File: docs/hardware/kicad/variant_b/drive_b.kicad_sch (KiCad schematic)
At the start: 11 parts, among them U40 74LVC08, U41 MDD20A front, U42 MDD20A rear, U43 CS FL, U44 CS FR, U45 CS RL, U46 CS RR

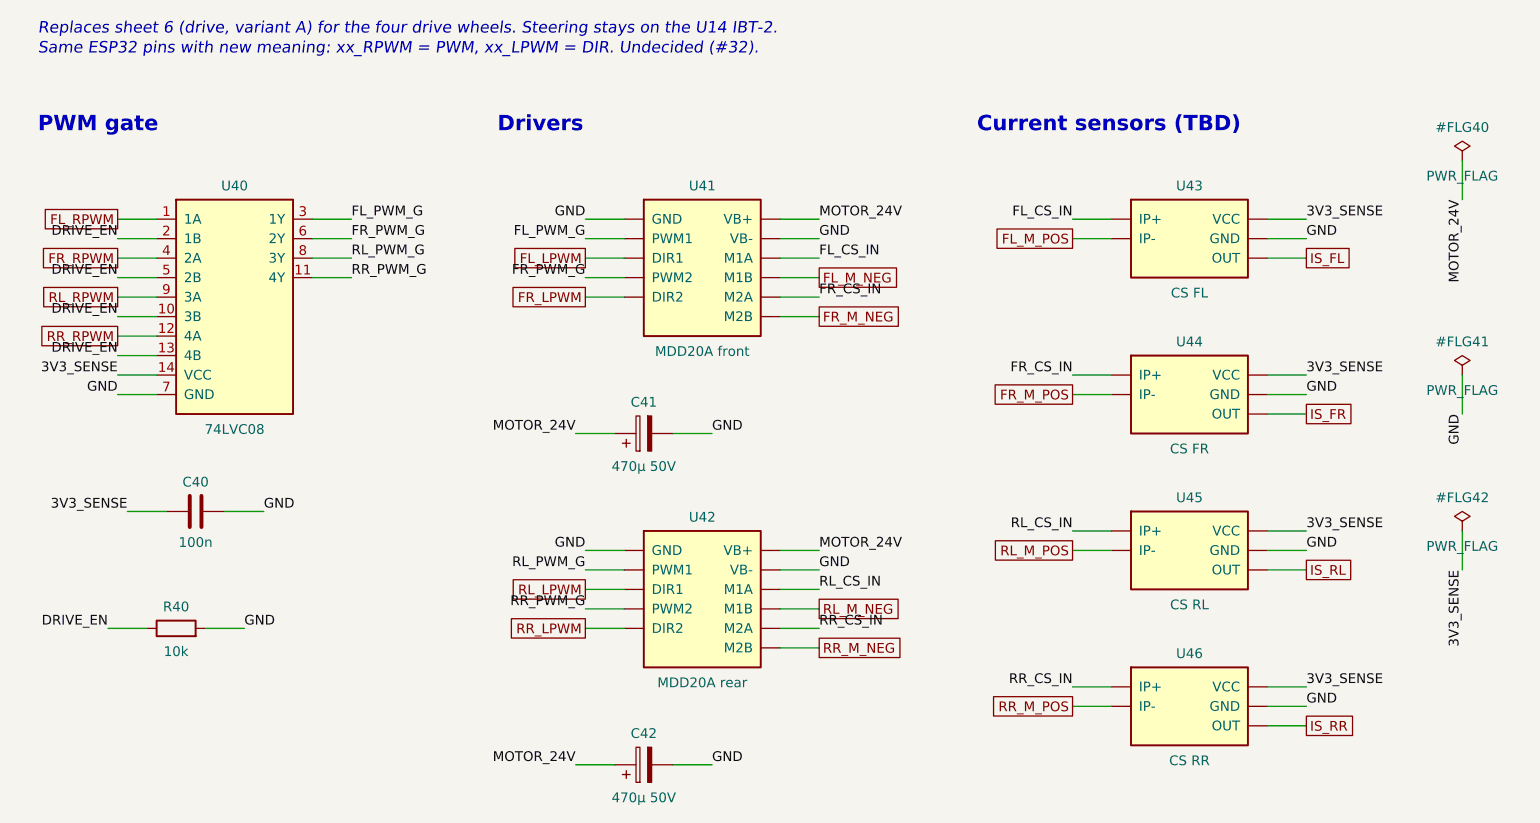
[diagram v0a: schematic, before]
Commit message: Safety gates follow the toy standards; add per-motor fuses F11-F14
SAFETY.md and COMMISSIONING.md now split their checks into required
(what a lab tests on every shop-bought ride-on: EN 71-1 / SI 562-1,
EN 62115, ASTM F963) and recommended (beyond any factory; a failure turns
the feature off instead of holding the project). New required checks:
key switch rating, a fuse per drive motor, a locked-wheel heat test, a
10 degree slope hold, top speed for the rider's age, and edges. The 0.75 s
link-loss stop stays required.

The schematic gets F11-F14, a 15 A placeholder blade fuse in each drive
motor's + lead inside the box, so a single stalled motor has a hardware
backstop below the 20 A software limit and the 40 A main fuse. Variant B's
current sensors feed the same fuses. Safety review updated to match.
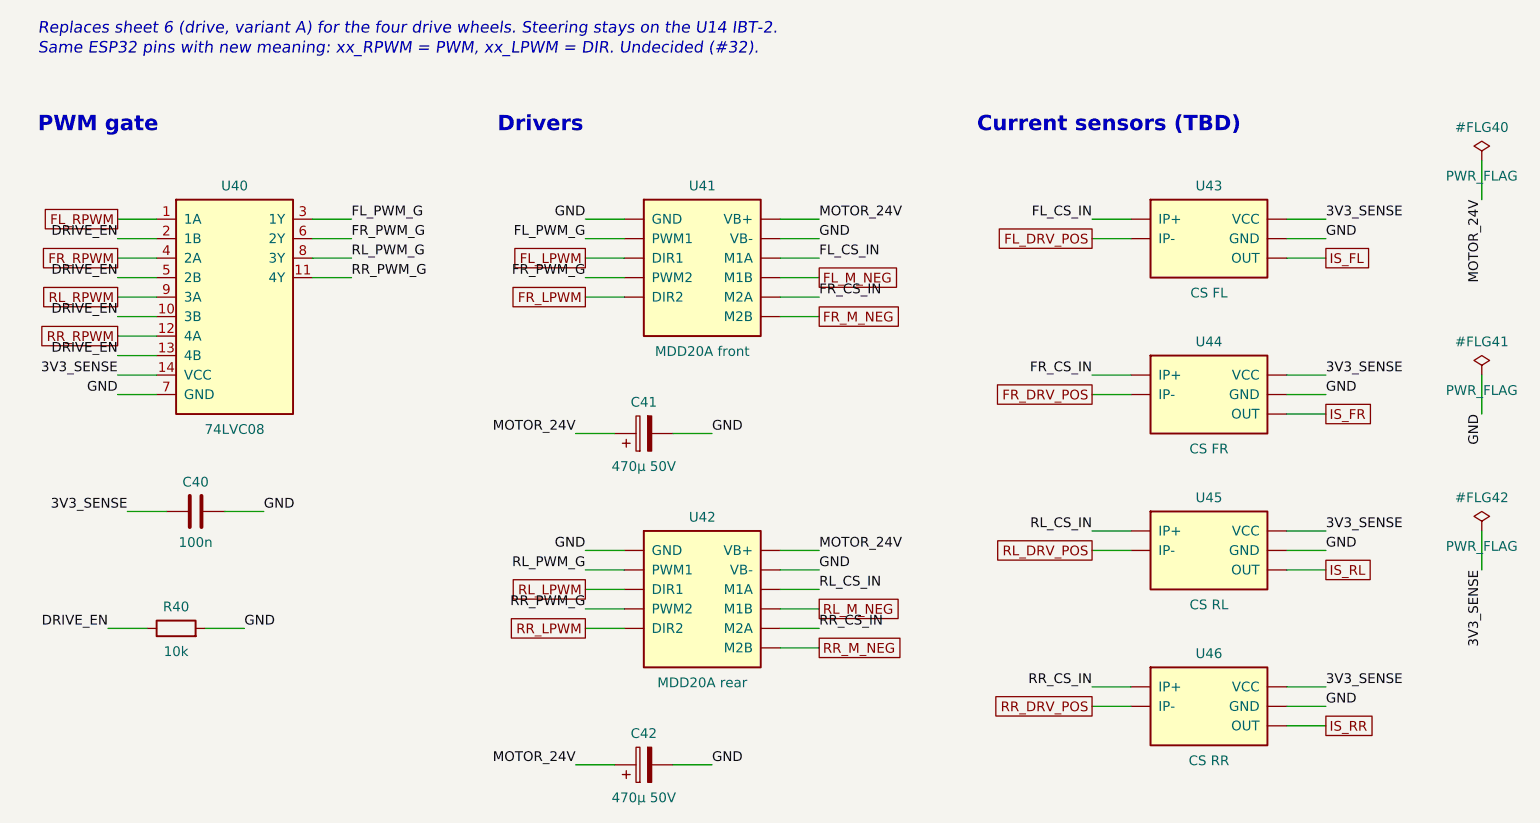
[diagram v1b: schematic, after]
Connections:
- net FL_M_POS renamed FL_DRV_POS
- net FR_M_POS renamed FR_DRV_POS
- net RL_M_POS renamed RL_DRV_POS
- net RR_M_POS renamed RR_DRV_POS
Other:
- moved on the sheet: U43, U44, U45, U46
